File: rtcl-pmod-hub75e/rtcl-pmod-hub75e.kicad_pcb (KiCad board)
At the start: 4 copper layers, 20 x 60 mm, 24 parts, among them J1 PMOD, J2 HIF3FC-16PA-2.54DSA(71), J3 Conn_01x02, U1 74LVC273, U2 74LVC273, U3 74LVC273, U4 74LVC273, U5 LM809M3-2.93, U6 74LVC2G86

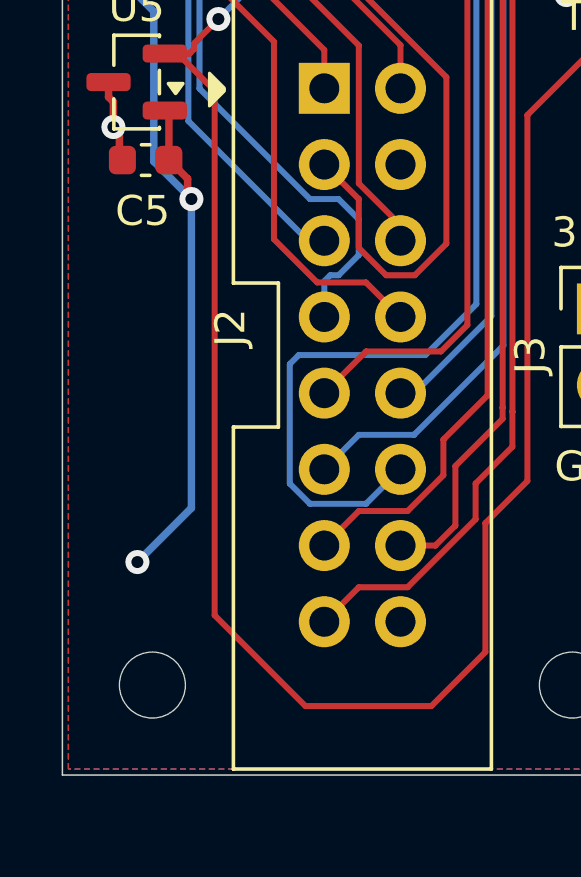
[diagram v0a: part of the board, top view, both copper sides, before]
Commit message: Update PCB and PRL files: adjust capacitor position and modify active layer settings
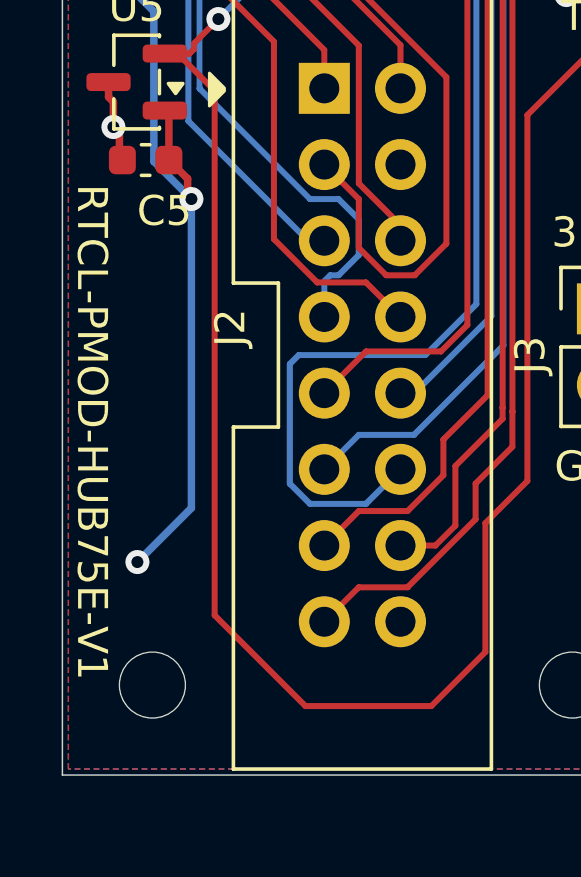
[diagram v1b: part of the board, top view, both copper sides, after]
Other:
- board text added: "RTCL-PMOD-HUB75E-V1"
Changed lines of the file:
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@@
 		(tags "capacitor")
 		(property "Reference" "C5"
-			(at -0.1 1.7 0)
+			(at 0.625 1.7 0)
 			(layer "F.SilkS")
 			(effects
@@
 		(layer "F.SilkS")
 		(effects
+			(font
+				(size 1 1)
+				(thickness 0.15)
+			)
+			(justify left bottom)
+		)
+	)
+	(gr_text "RTCL-PMOD-HUB75E-V1"
+		(at 100.4 90.3 270)
+		(layer "F.SilkS")
+		(effects

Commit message: wip
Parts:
- J2: value HIF3FC-16PA-2.54DSA(71) -> HUB75E
- U6: value 74LVC2G86 -> SN74LVC2G86DCUR
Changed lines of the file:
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@@
 			)
 		)
-		(property "Value" "HIF3FC-16PA-2.54DSA(71)"
+		(property "Value" "HUB75E"
 			(at 1.27 21.5 0)
 			(layer "F.Fab")
@@
 			)
 		)
-		(property "Value" "74LVC2G86"
+		(property "Value" "SN74LVC2G86DCUR"
 			(at 0 1.95 0)
 			(layer "F.Fab")

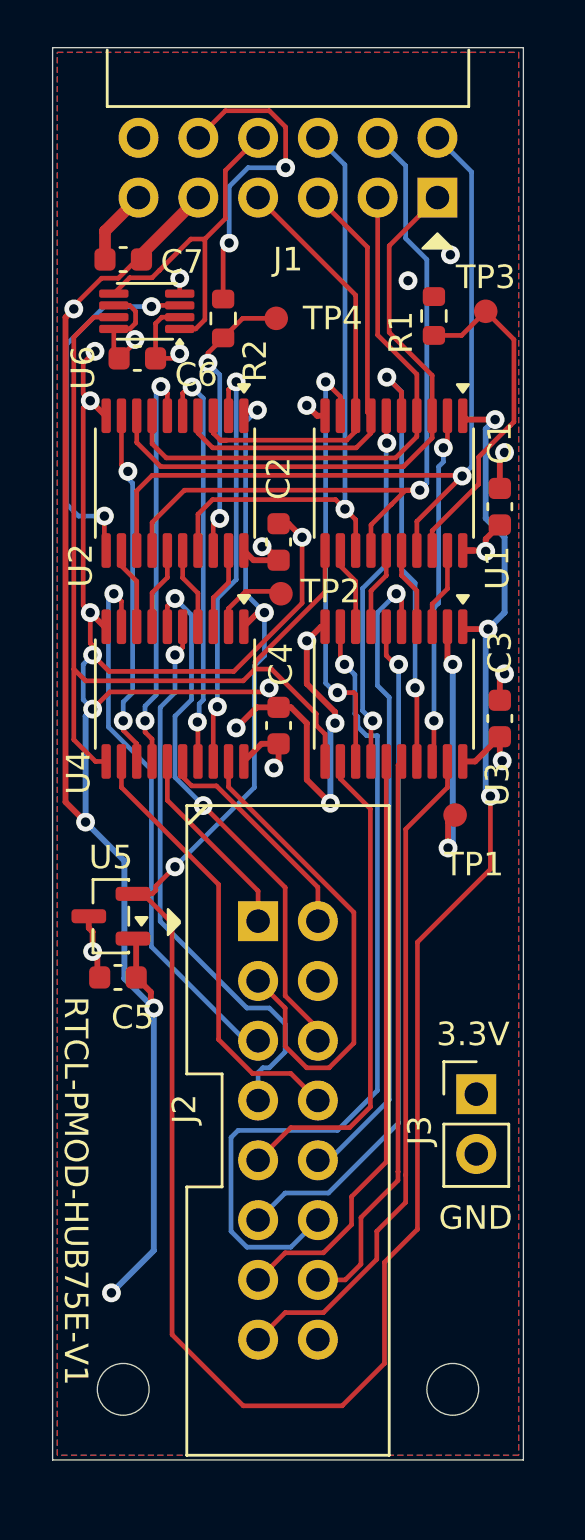
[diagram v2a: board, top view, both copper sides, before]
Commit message: Add new footprints for SPDT switch and OS102011MS2QN1 switch
- Created a new footprint for SPDT switch (SPDT_OS102011_CNK) with detailed pad and silk layer definitions.
- Added a new footprint for OS102011MS2QN1 switch, including properties, pads, and 3D model reference.
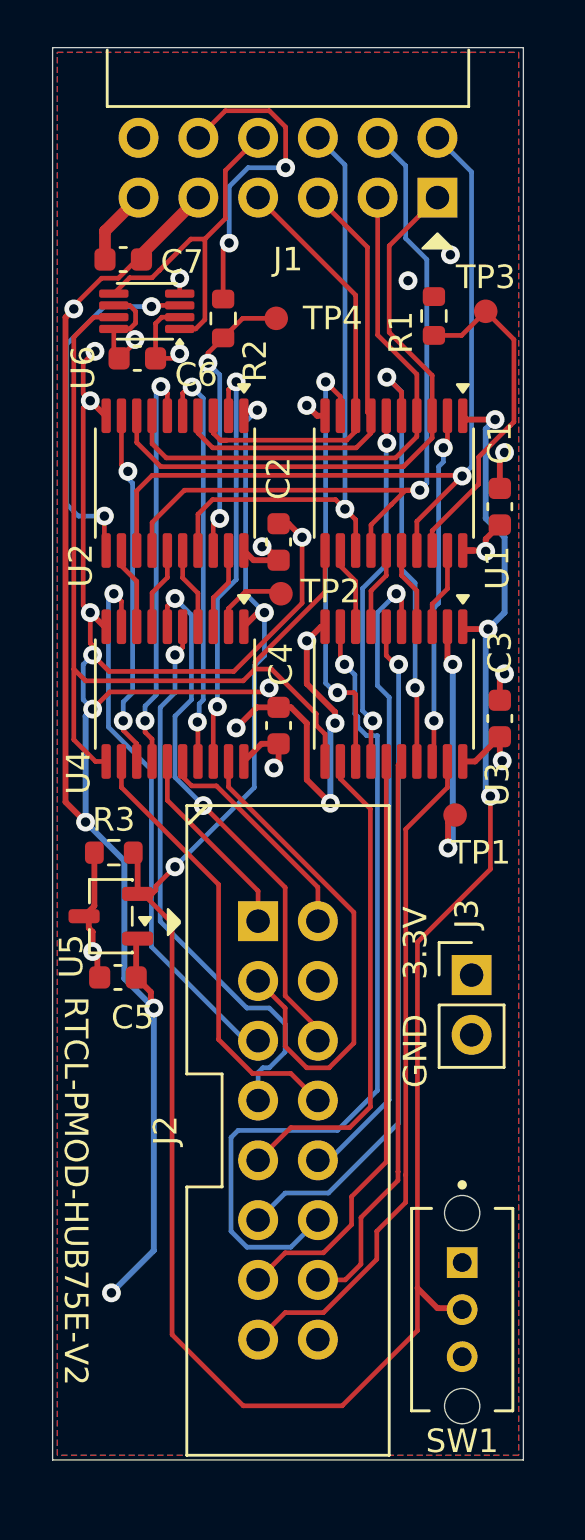
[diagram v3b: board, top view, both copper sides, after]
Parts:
- removed REF** (x2): MountingHole_2.2mm_M2, MountingHole:MountingHole_2.2mm_M2
- added R3: 10k, Resistor_SMD:R_0603_1608Metric, F.Cu at (102.6, 84.2)
- added SW1: OS102011MS2QN1, rtcl-pmod-hub75e:SW_OS102011MS2QN1, F.Cu at (117.4, 103.6)
- U5: value LM809M3-2.93 -> APX803D-29SAG-7; footprint Package_TO_SOT_SMD:SOT-23 -> Package_TO_SOT_SMD:SOT-23-3
- moved J3 5.06 mm to (117.8, 89.4)
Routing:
- net /RESET: track 101.8 -> 105.8 mm
- net +3.3V: track 22.4 -> 25.3 mm
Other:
- board text added: "RTCL-PMOD-HUB75E-V2"
- board text removed: "RTCL-PMOD-HUB75E-V1"

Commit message: Update active layer in rtcl-pmod-hub75e.kicad_prl from 5 to 1
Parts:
- added REF**: MountingHole_2.2mm_M2, MountingHole:MountingHole_2.2mm_M2, F.Cu at (103.0, 107.0)
- added REF**: MountingHole_2.2mm_M2, MountingHole:MountingHole_2.2mm_M2, F.Cu at (117.0, 107.0)
- moved SW1 5.61 mm to (117.4, 98.0)
- moved J3 2.40 mm to (117.8, 87.0)
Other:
- board text added: "© RTC-Lab"
